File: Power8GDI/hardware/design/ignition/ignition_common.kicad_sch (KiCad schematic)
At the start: 18 parts, among them U5400 SN74LVC1G17QDBVRQ1, U5401 SN74LVC1G11BDCKRQ1, U5402 UCC27524AQDRQ1, U5403 UCC27524AQDRQ1, U5404 UCC27524AQDRQ1, U5405 UCC27524AQDRQ1

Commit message: Integrate sequenced logic supply and four protected motor bridges
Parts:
- U5400: symbol Power8GDI_Core:SN74LVC1G17_Q1 -> Power8GDI_Core:IGN_SN74LVC1G17_Q1
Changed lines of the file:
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@@
 (text "PASSIVE PRIMARY OUTPUT ASSEMBLY" (at 25 20 0) (effects (font (size 2 2)) (justify left top)))
 (text "IGN_OC_OK is open drain, healthy high. Parent connects to HW_KILL_N.\nNo firmware-only current limit. Fault turn-off can cause an unintended spark.\nCoil +12V feed must be removed on fault; see HW_IGNITION_B58.md." (at 25 35 0) (effects (font (size 1.27 1.27)) (justify left top)))
-(symbol (lib_id "Power8GDI_Core:SN74LVC1G17_Q1") (at 100.33 90.17 0) (unit 1) (in_bom yes) (on_board yes) (dnp no) (property "Reference" "U5400" (at 100.33 82.55 0) (effects (font (size 1.27 1.27)))) (property "Value" "SN74LVC1G17QDBVRQ1" (at 100.33 97.79 0) (effects (font (size 1.27 1.27)))) (property "Footprint" "Package_TO_SOT_SMD:SOT-23-5" (at 100.33 90.17 0) (effects (font (size 1.27 1.27)) (hide yes))) (property "Design note" "" (at 100.33 90.17 0) (effects (font (size 1.27 1.27)) (hide yes))) (pin "1") (pin "2") (pin "3") (pin "4") (pin "5") (instances (project "Power8GDI_Core" (path "/f4d21065-0a5b-5086-a08e-1af9469f04bd/3f8231a8-69f9-55dc-b640-4840d30367f8" (reference "U5400") (unit 1)))))
+(symbol (lib_id "Power8GDI_Core:IGN_SN74LVC1G17_Q1") (at 100.33 90.17 0) (unit 1) (in_bom yes) (on_board yes) (dnp no) (property "Reference" "U5400" (at 100.33 82.55 0) (effects (font (size 1.27 1.27)))) (property "Value" "SN74LVC1G17QDBVRQ1" (at 100.33 97.79 0) (effects (font (size 1.27 1.27)))) (property "Footprint" "Package_TO_SOT_SMD:SOT-23-5" (at 100.33 90.17 0) (effects (font (size 1.27 1.27)) (hide yes))) (property "Design note" "" (at 100.33 90.17 0) (effects (font (size 1.27 1.27)) (hide yes))) (pin "1") (pin "2") (pin "3") (pin "4") (pin "5") (instances (project "Power8GDI_Core" (path "/f4d21065-0a5b-5086-a08e-1af9469f04bd/3f8231a8-69f9-55dc-b640-4840d30367f8" (reference "U5400") (unit 1)))))
 (no_connect (at 80.01 85.09))
 (wire (pts (xy 80.01 90.17) (xy 72.39 90.17)) (stroke (width 0) (type default)))

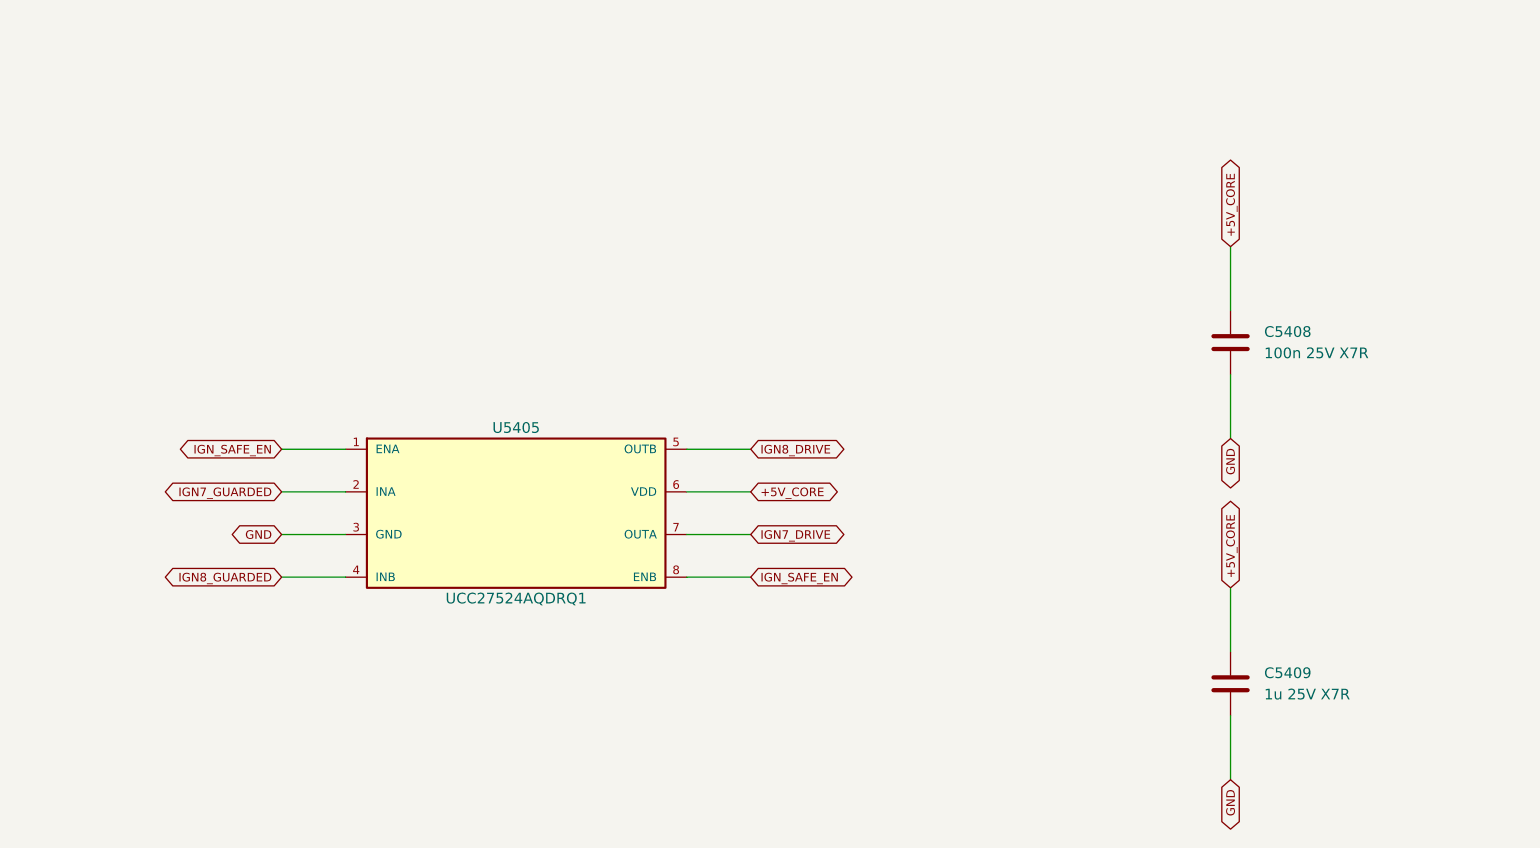
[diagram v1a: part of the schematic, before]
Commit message: Redesign sport target as six DI/PI channels with two motors and one lambda
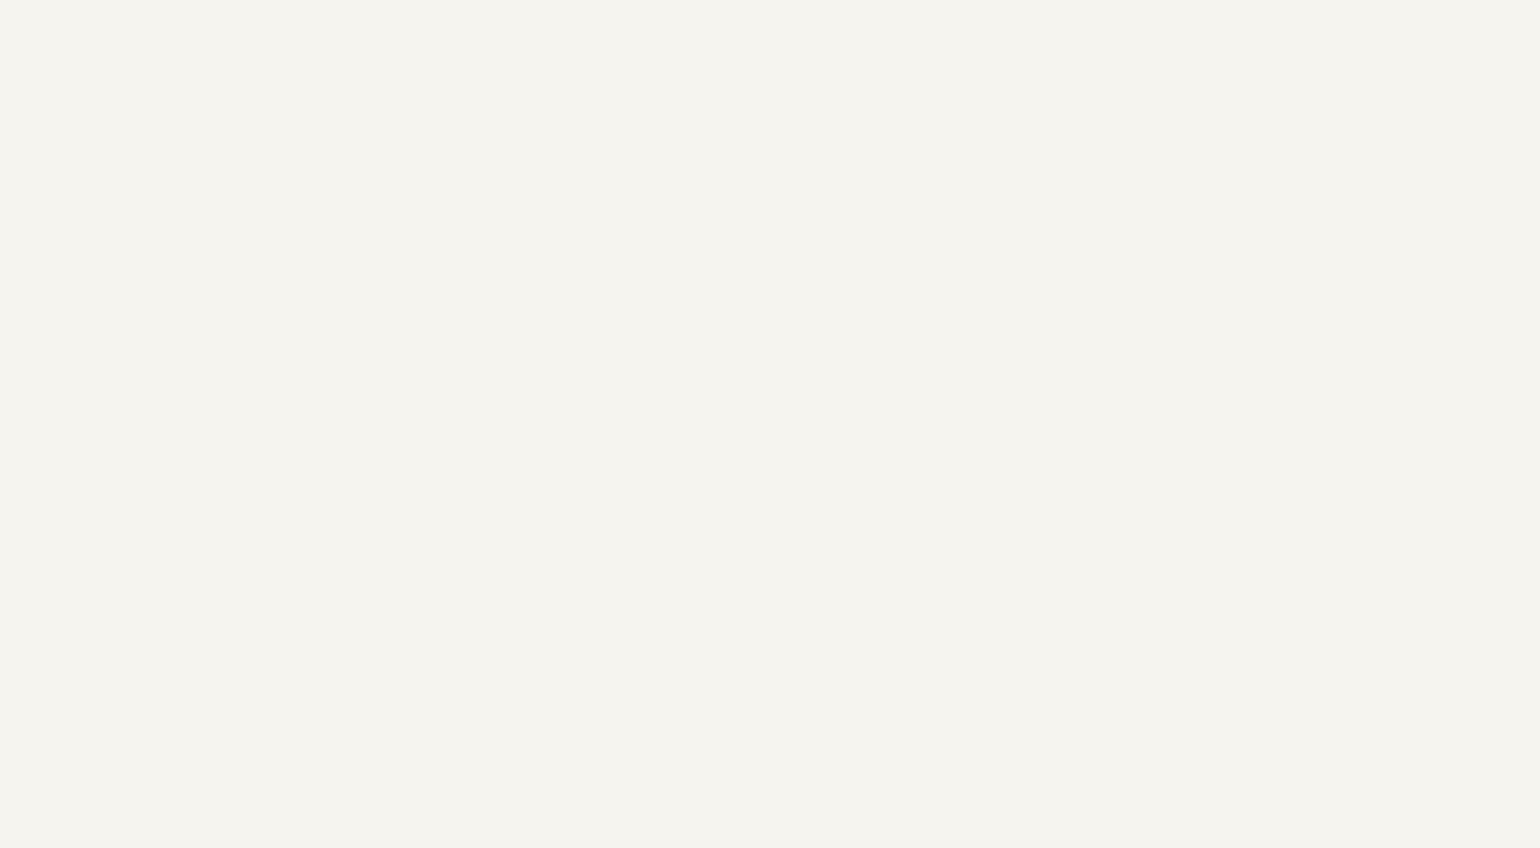
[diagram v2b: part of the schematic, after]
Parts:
- removed C5408: 100n 25V X7R, Capacitor_SMD:C_0603_1608Metric, symbol Power8GDI_Core:C
- removed C5409: 1u 25V X7R, Capacitor_SMD:C_0603_1608Metric, symbol Power8GDI_Core:C
- removed U5405: UCC27524AQDRQ1, Package_SO:SOIC-8_3.9x4.9mm_P1.27mm, symbol Power8GDI_Core:UCC27524AQDRQ1
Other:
- title: Ignition permission and four dual gate drivers -> Ignition permission and three dual gate drivers
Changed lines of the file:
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@@
-(kicad_sch (version 20250114) (generator "eeschema") (paper "A2") (title_block (title "Ignition permission and four dual gate drivers") (rev "Engineering draft 0.1") (comment 1 "UNQUALIFIED: no manufacturing or engine approval"))
+(kicad_sch (version 20250114) (generator "eeschema") (paper "A2") (title_block (title "Ignition permission and three dual gate drivers") (rev "Engineering draft 0.1") (comment 1 "UNQUALIFIED: no manufacturing or engine approval"))
 (text "PASSIVE PRIMARY OUTPUT ASSEMBLY" (at 25 20 0) (effects (font (size 2 2)) (justify left top)))
 (text "IGN_OC_OK is open drain, healthy high. Parent connects to HW_KILL_N.\nNo firmware-only current limit. Fault turn-off can cause an unintended spark.\nCoil +12V feed must be removed on fault; see HW_IGNITION_B58.md." (at 25 35 0) (effects (font (size 1.27 1.27)) (justify left top)))
@@
 (wire (pts (xy 195.58 334.01) (xy 195.58 341.63)) (stroke (width 0) (type default)))
 (global_label "GND" (shape bidirectional) (at 195.58 341.63 90) (effects (font (size 1.016 1.016)) (justify right bottom)))
-(symbol (lib_id "Power8GDI_Core:UCC27524AQDRQ1") (at 379.73 309.88 0) (unit 1) (in_bom yes) (on_board yes) (dnp no) (property "Reference" "U5405" (at 379.73 299.72 0) (effects (font (size 1.27 1.27)))) (property "Value" "UCC27524AQDRQ1" (at 379.73 320.04 0) (effects (font (size 1.27 1.27)))) (property "Footprint" "Package_SO:SOIC-8_3.9x4.9mm_P1.27mm" (at 379.73 309.88 0) (effects (font (size 1.27 1.27)) (hide yes))) (property "Design note" "Automotive grade 1; SOIC-8 D package (not PowerPAD DGN). UVLO holds outputs low. 5A is peak gate drive, not coil current." (at 379.73 309.88 0) (effects (font (size 1.27 1.27)) (hide yes))) (pin "1") (pin "2") (pin "3") (pin "4") (pin "5") (pin "6") (pin "7") (pin "8") (instances (project "Power8GDI_Core" (path "/f4d21065-0a5b-5086-a08e-1af9469f04bd/3f8231a8-69f9-55dc-b640-4840d30367f8" (reference "U5405") (unit 1)))))
-(wire (pts (xy 359.41 302.26) (xy 351.79 302.26)) (stroke (width 0) (type default)))
-(global_label "IGN_SAFE_EN" (shape bidirectional) (at 351.79 302.26 0) (effects (font (size 1.016 1.016)) (justify right bottom)))
-(wire (pts (xy 359.41 307.34) (xy 351.79 307.34)) (stroke (width 0) (type default)))
-(global_label "IGN7_GUARDED" (shape bidirectional) (at 351.79 307.34 0) (effects (font (size 1.016 1.016)) (justify right bottom)))
-(wire (pts (xy 359.41 312.42) (xy 351.79 312.42)) (stroke (width 0) (type default)))
-(global_label "GND" (shape bidirectional) (at 351.79 312.42 0) (effects (font (size 1.016 1.016)) (justify right bottom)))
-(wire (pts (xy 359.41 317.5) (xy 351.79 317.5)) (stroke (width 0) (type default)))
-(global_label "IGN8_GUARDED" (shape bidirectional) (at 351.79 317.5 0) (effects (font (size 1.016 1.016)) (justify right bottom)))
-(wire (pts (xy 400.05 302.26) (xy 407.67 302.26)) (stroke (width 0) (type default)))
-(global_label "IGN8_DRIVE" (shape bidirectional) (at 407.67 302.26 180) (effects (font (size 1.016 1.016)) (justify left bottom)))
-(wire (pts (xy 400.05 307.34) (xy 407.67 307.34)) (stroke (width 0) (type default)))
-(global_label "+5V_CORE" (shape bidirectional) (at 407.67 307.34 180) (effects (font (size 1.016 1.016)) (justify left bottom)))
-(wire (pts (xy 400.05 312.42) (xy 407.67 312.42)) (stroke (width 0) (type default)))
-(global_label "IGN7_DRIVE" (shape bidirectional) (at 407.67 312.42 180) (effects (font (size 1.016 1.016)) (justify left bottom)))
-(wire (pts (xy 400.05 317.5) (xy 407.67 317.5)) (stroke (width 0) (type default)))
-(global_label "IGN_SAFE_EN" (shape bidirectional) (at 407.67 317.5 180) (effects (font (size 1.016 1.016)) (justify left bottom)))
-(symbol (lib_id "Power8GDI_Core:C") (at 464.82 289.56 0) (unit 1) (in_bom yes) (on_board yes) (dnp no) (property "Reference" "C5408" (at 468.82 288.29 0) (effects (font (size 1.27 1.27)) (justify left))) (property "Value" "100n 25V X7R" (at 468.82 290.83 0) (effects (font (size 1.27 1.27)) (justify left))) (property "Footprint" "Capacitor_SMD:C_0603_1608Metric" (at 464.82 289.56 0) (effects (font (size 1.27 1.27)) (hide yes))) (property "Design note" "" (at 464.82 289.56 0) (effects (font (size 1.27 1.27)) (hide yes))) (pin "1") (pin "2") (instances (project "Power8GDI_Core" (path "/f4d21065-0a5b-5086-a08e-1af9469f04bd/3f8231a8-69f9-55dc-b640-4840d30367f8" (reference "C5408") (unit 1)))))
-(wire (pts (xy 464.82 285.75) (xy 464.82 278.13)) (stroke (width 0) (type default)))
-(global_label "+5V_CORE" (shape bidirectional) (at 464.82 278.13 270) (effects (font (size 1.016 1.016)) (justify left bottom)))
-(wire (pts (xy 464.82 293.37) (xy 464.82 300.99)) (stroke (width 0) (type default)))
-(global_label "GND" (shape bidirectional) (at 464.82 300.99 90) (effects (font (size 1.016 1.016)) (justify right bottom)))
-(symbol (lib_id "Power8GDI_Core:C") (at 464.82 330.2 0) (unit 1) (in_bom yes) (on_board yes) (dnp no) (property "Reference" "C5409" (at 468.82 328.93 0) (effects (font (size 1.27 1.27)) (justify left))) (property "Value" "1u 25V X7R" (at 468.82 331.47 0) (effects (font (size 1.27 1.27)) (justify left))) (property "Footprint" "Capacitor_SMD:C_0603_1608Metric" (at 464.82 330.2 0) (effects (font (size 1.27 1.27)) (hide yes))) (property "Design note" "" (at 464.82 330.2 0) (effects (font (size 1.27 1.27)) (hide yes))) (pin "1") (pin "2") (instances (project "Power8GDI_Core" (path "/f4d21065-0a5b-5086-a08e-1af9469f04bd/3f8231a8-69f9-55dc-b640-4840d30367f8" (reference "C5409") (unit 1)))))
-(wire (pts (xy 464.82 326.39) (xy 464.82 318.77)) (stroke (width 0) (type default)))
-(global_label "+5V_CORE" (shape bidirectional) (at 464.82 318.77 270) (effects (font (size 1.016 1.016)) (justify left bottom)))
-(wire (pts (xy 464.82 334.01) (xy 464.82 341.63)) (stroke (width 0) (type default)))
-(global_label "GND" (shape bidirectional) (at 464.82 341.63 90) (effects (font (size 1.016 1.016)) (justify right bottom)))
 (sheet_instances (path "/" (page "1"))))

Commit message: Review B58 injector power stage and bind selected GDI6 BOM
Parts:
- C5400, C5401, C5402, C5404, C5406: Hardware_Qualification (none) -> BOARD_QUALIFICATION_PENDING; MPN (none) -> C0603C104K5RACTU; Manufacturer (none) -> KEMET; Procurement_Status (none) -> SELECTED_CATALOG_ITEM; Purchase_Released (none) -> false; Selection_Gaps (none) -> []; Selection_ID (none) -> SEL-6bf9727c4e40; Selection_Ratings (none) -> {"capacitance_pf": 100000, "dielectric": "X7R", "rated_volt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; Selection_Source_URLs (none) -> https://search.kemet.com/download/specsheet/C0603C104K5RACTU
- C5403, C5405, C5407: Hardware_Qualification (none) -> BOARD_QUALIFICATION_PENDING; MPN (none) -> C0603C105K3RACTU; Manufacturer (none) -> KEMET; Procurement_Status (none) -> SELECTED_CATALOG_ITEM; Purchase_Released (none) -> false; Selection_Gaps (none) -> []; Selection_ID (none) -> SEL-4bca20b134b8; Selection_Ratings (none) -> {"capacitance_pf": 1000000, "dc_bias_qualification": "PENDI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; Selection_Source_URLs (none) -> https://search.kemet.com/download/specsheet/C0603C105K3RACTU
- R5400: Hardware_Qualification (none) -> BOARD_QUALIFICATION_PENDING; MPN (none) -> CRCW060310K0FKEA; Manufacturer (none) -> Vishay; Procurement_Status (none) -> SELECTED_FAMILY_CODE; Purchase_Released (none) -> false; Selection_Gaps (none) -> []; Selection_ID (none) -> SEL-9c0806476875; Selection_Ratings (none) -> {"aec_q200": true, "derating": "Use manufacturer power vers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; Selection_Source_URLs (none) -> https://www.vishay.com/docs/20035/dcrcwe3.pdf
- R5401: Hardware_Qualification (none) -> BOARD_QUALIFICATION_PENDING; MPN (none) -> CRCW06031K00FKEA; Manufacturer (none) -> Vishay; Procurement_Status (none) -> SELECTED_FAMILY_CODE; Purchase_Released (none) -> false; Selection_Gaps (none) -> []; Selection_ID (none) -> SEL-38197231a947; Selection_Ratings (none) -> {"aec_q200": true, "derating": "Use manufacturer power vers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; Selection_Source_URLs (none) -> https://www.vishay.com/docs/20035/dcrcwe3.pdf
- U5400: Hardware_Qualification (none) -> PINOUT_RATINGS_AND_DELIVERY_SUFFIX_REVIEW_PENDING; MPN (none) -> SN74LVC1G17QDBVRQ1; Manufacturer (none) -> Texas Instruments; Procurement_Status (none) -> REFERENCE_MPN_RETAINED; Purchase_Released (none) -> false; Selection_Gaps (none) -> ["Existing schematic MPN retained. Complete circuit rating/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; Selection_ID (none) -> SEL-ecf3e6662afb; Selection_Ratings (none) -> {}; Selection_Source_URLs (none) -> https://www.ti.com/product/SN74LVC1G17-Q1/part-details/SN74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
- U5401: Hardware_Qualification (none) -> PINOUT_RATINGS_AND_DELIVERY_SUFFIX_REVIEW_PENDING; MPN (none) -> SN74LVC1G11BDCKRQ1; Manufacturer (none) -> Texas Instruments; Procurement_Status (none) -> REFERENCE_MPN_RETAINED; Purchase_Released (none) -> false; Selection_Gaps (none) -> ["Existing schematic MPN retained. Complete circuit rating/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; Selection_ID (none) -> SEL-af3da1e13ada; Selection_Ratings (none) -> {}; Selection_Source_URLs (none) -> https://www.ti.com/product/SN74LVC1G11B-Q1/part-details/SN7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
- U5402, U5403, U5404: Hardware_Qualification (none) -> PINOUT_RATINGS_AND_DELIVERY_SUFFIX_REVIEW_PENDING; MPN (none) -> UCC27524AQDRQ1; Manufacturer (none) -> Texas Instruments; Procurement_Status (none) -> REFERENCE_MPN_RETAINED; Purchase_Released (none) -> false; Selection_Gaps (none) -> ["Existing schematic MPN retained. Complete circuit rating/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; Selection_ID (none) -> SEL-cf9971f5fc4e; Selection_Ratings (none) -> {}; Selection_Source_URLs (none) -> https://www.ti.com/product/UCC27524A-Q1/part-details/UCC275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
